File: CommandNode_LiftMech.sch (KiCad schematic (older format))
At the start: 0 parts

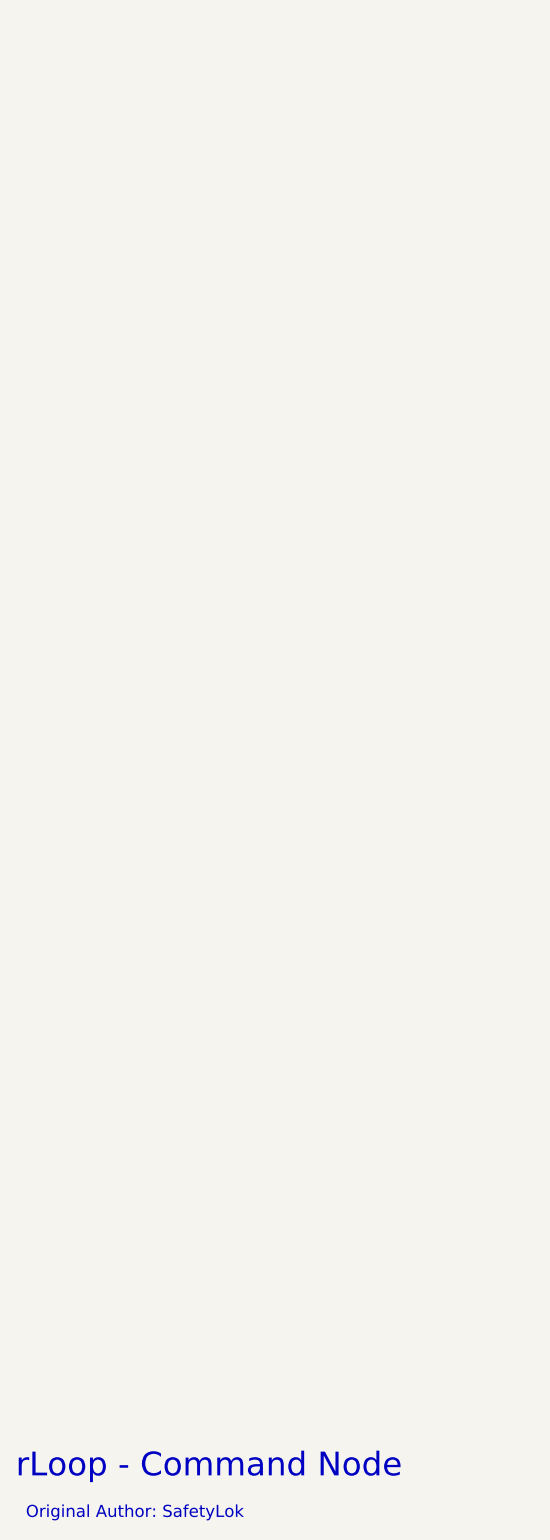
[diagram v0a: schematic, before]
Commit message: Created isolated RS585 interfaces and completed park brake.
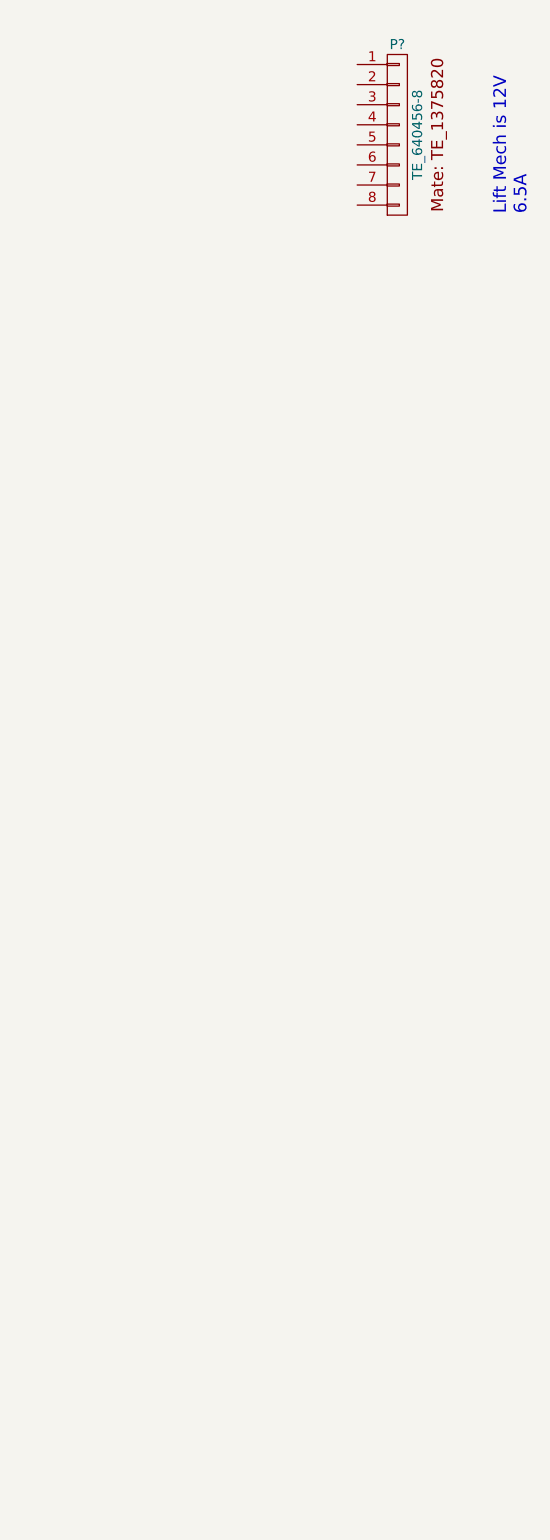
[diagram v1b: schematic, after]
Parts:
- added P?: TE_640456-8, RLOOP_FOOTPRINTS:rLoop_TE640456-8, symbol TE_640456-8
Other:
- note added: "Lift Mech is 12V\n6.5A"
- note removed: "Original Author: SafetyLok"
- note removed: "rLoop - Command Node"
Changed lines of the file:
@@
 LIBS:contrib
 LIBS:valves
+LIBS:rloop
 LIBS:CommandNode-cache
 EELAYER 25 0
@@
 $Descr A3 16535 11693
 encoding utf-8
-Sheet 3 4
-Title "Hover Engine Interface"
+Sheet 5 7
+Title "Lift Mechanism"
 Date ""
 Rev "1"
@@
 Comment4 ""
 $EndDescr
-Text Notes 11900 10200 0    118  ~ 0
-rLoop - Command Node
-Text Notes 11950 10400 0    60   ~ 0
-Original Author: SafetyLok
+$Comp
+L TE_640456-8 P?
+U 1 1 575DB937
+P 13750 3100
+F 0 "P?" H 13800 3150 50  0000 C CNN
+F 1 "TE_640456-8" V 13900 2700 50  0000 C CNN
+F 2 "RLOOP_FOOTPRINTS:rLoop_TE640456-8" H 13800 2700 50  0001 C CNN
+F 3 "" H 13800 2700 50  0000 C CNN
+	1    13750 3100
+	1    0    0    -1
+$EndComp
+Text Notes 14450 3900 1    63   ~ 0
+Lift Mech is 12V\n6.5A
 $EndSCHEMATC

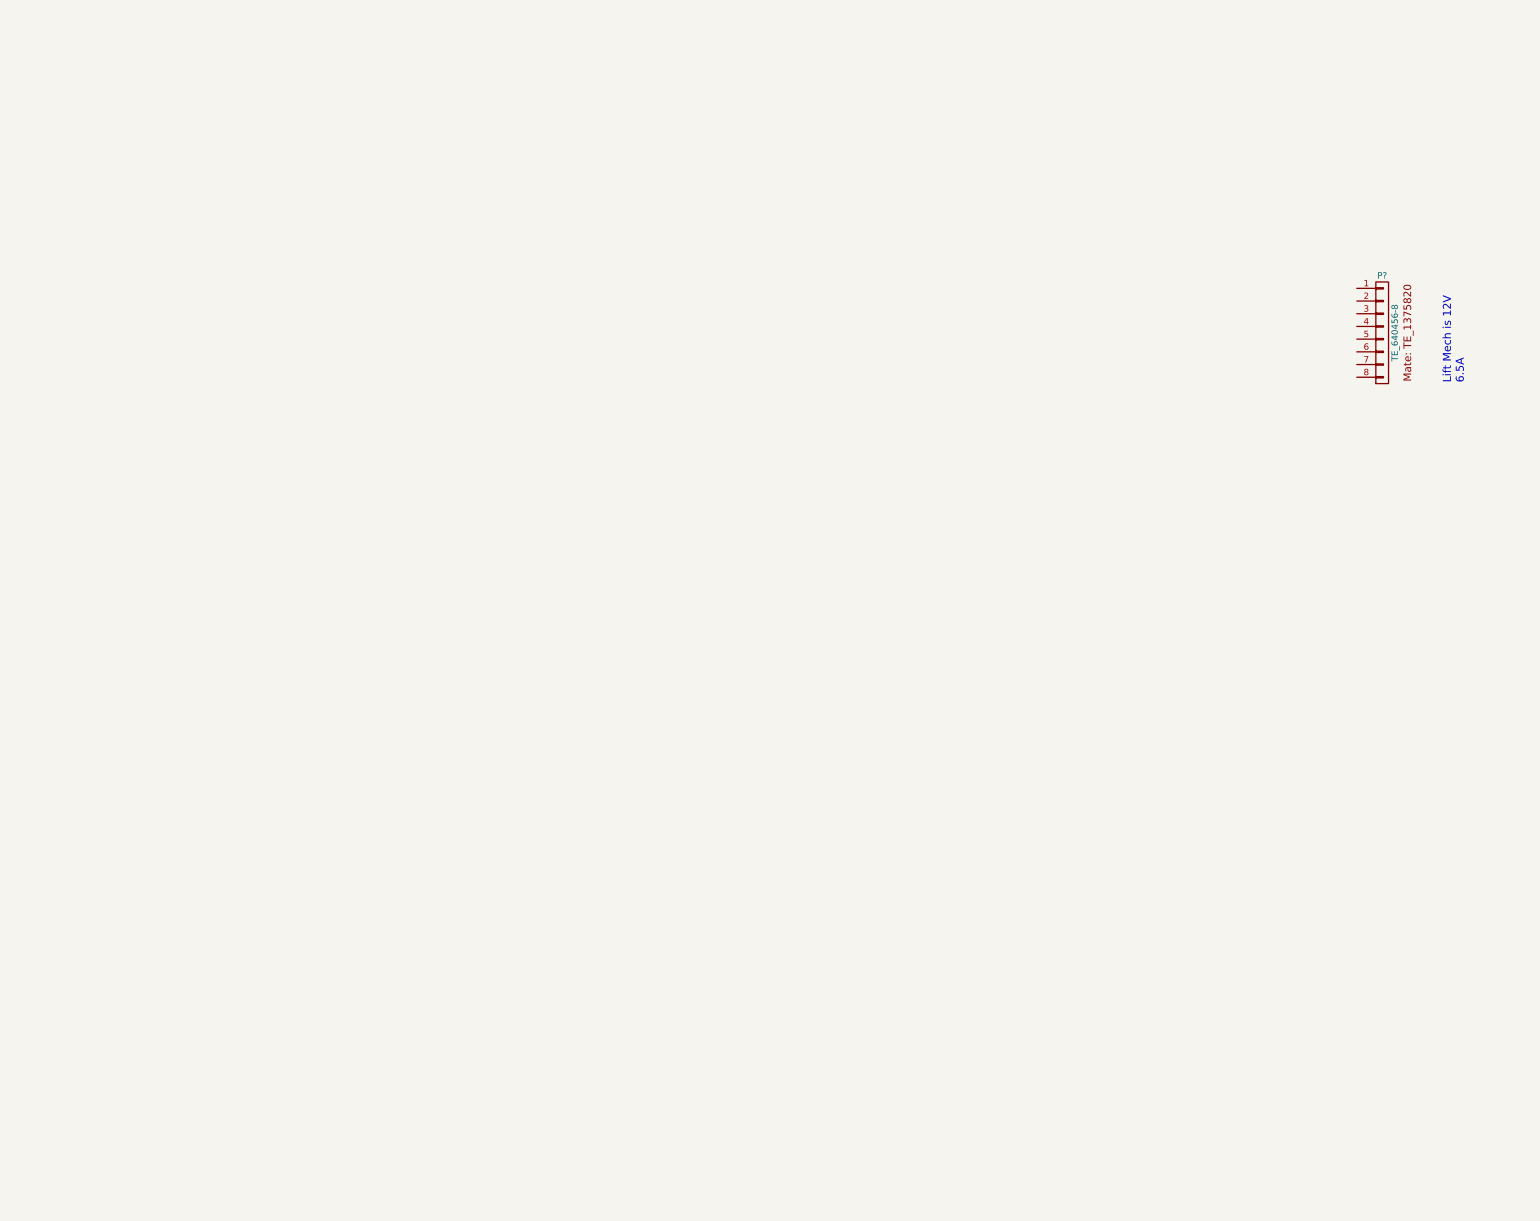
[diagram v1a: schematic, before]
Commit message: Finish and print schematics for review
Lifting mechanism, charger interface, Data Enable on HE controller
RS585, Park Brake and node core.
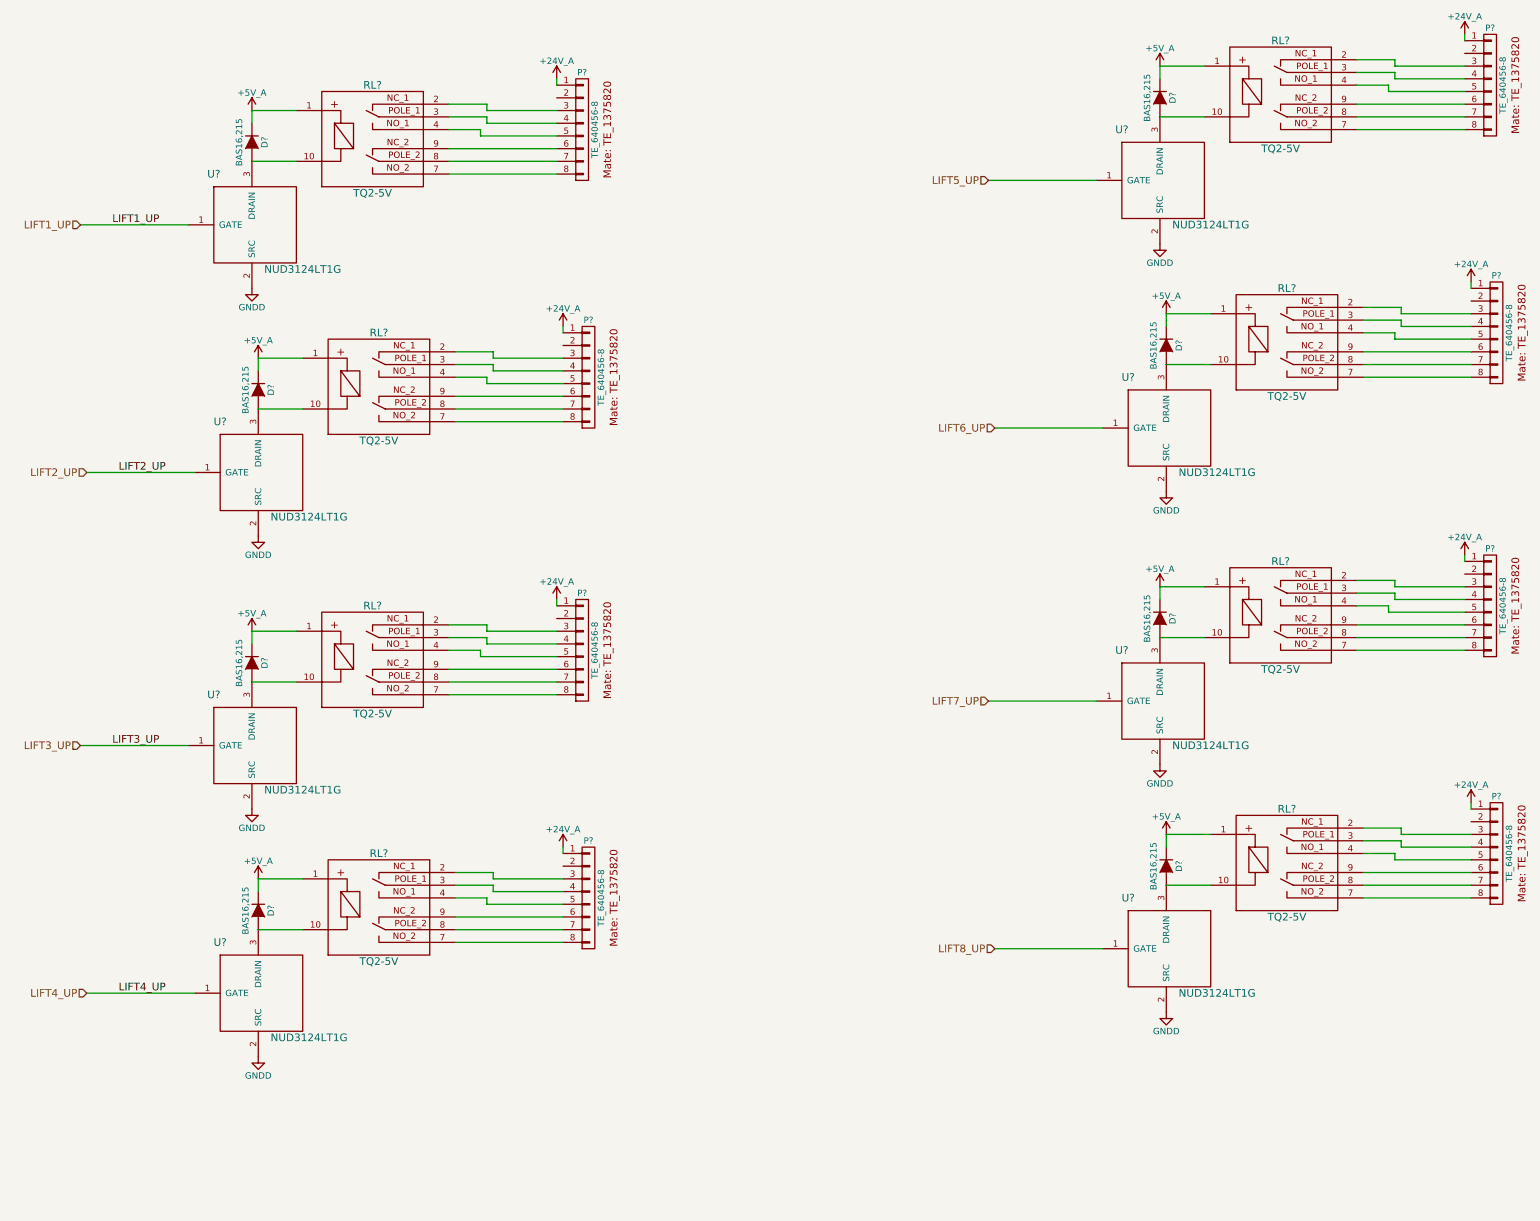
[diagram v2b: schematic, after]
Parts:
- added D? (x8): BAS16,215, RLOOP_FOOTPRINTS:rLoop_SOT23, symbol BAS16,215
- added P? (x7): TE_640456-8, RLOOP_FOOTPRINTS:rLoop_TE640456-8, symbol TE_640456-8
- added RL? (x8): TQ2-5V, RLOOP_FOOTPRINTS:rLoop_DIP10, symbol TQ2-5V
- added U? (x8): NUD3124LT1G, RLOOP_FOOTPRINTS:rLoop_SOT23, symbol NUD3124LT1G
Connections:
- net +5V: now reaches P?.1 (P1)
- net +5V: now also D?.3 (K), D?.3 (K), D?.3 (K), D?.3 (K), D?.3 (K), D?.3 (K), D?.3 (K), D?.3 (K), P?.1 (P1), P?.1 (P1), P?.1 (P1), P?.1 (P1), P?.1 (P1), P?.1 (P1), P?.1 (P1), RL?.1, RL?.1, RL?.1, RL?.1, RL?.1, RL?.1, RL?.1, RL?.1
- net at P?.3 (P3): now also RL?.2
- net at P?.4 (P4): now also RL?.3
- net at P?.5 (P5): now also RL?.4
- net at P?.6 (P6): now also RL?.9
- net at P?.7 (P7): now also RL?.8
- net at P?.8 (P8): now also RL?.7
- new net: D?.1 (A), RL?.10, U?.3 (DRAIN) (x8)
- new net: P?.3 (P3), RL?.2 (x7)
- new net: P?.4 (P4), RL?.3 (x7)
- new net: P?.5 (P5), RL?.4 (x7)
- new net: P?.6 (P6), RL?.9 (x7)
- new net: P?.7 (P7), RL?.8 (x7)
- new net: P?.8 (P8), RL?.7 (x7)
- new net GNDD: U?.2 (SRC), U?.2 (SRC), U?.2 (SRC), U?.2 (SRC), U?.2 (SRC), U?.2 (SRC), U?.2 (SRC), U?.2 (SRC)
- new net LIFT1_UP: U?.1 (GATE)
- new net LIFT2_UP: U?.1 (GATE)
- new net LIFT3_UP: U?.1 (GATE)
- new net LIFT4_UP: U?.1 (GATE)
- new net LIFT5_UP: U?.1 (GATE)
- new net LIFT6_UP: U?.1 (GATE)
- new net LIFT7_UP: U?.1 (GATE)
- new net LIFT8_UP: U?.1 (GATE)
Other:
- note removed: "Lift Mech is 12V\n6.5A"
- moved on the sheet: P?
